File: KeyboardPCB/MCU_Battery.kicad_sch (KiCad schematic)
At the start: 22 parts, among them U1 ATmega32U4-M, U2 TPS61222DCK, U3 MCP73831-2-OT, Y1 XRCGB16M000FXN02R0

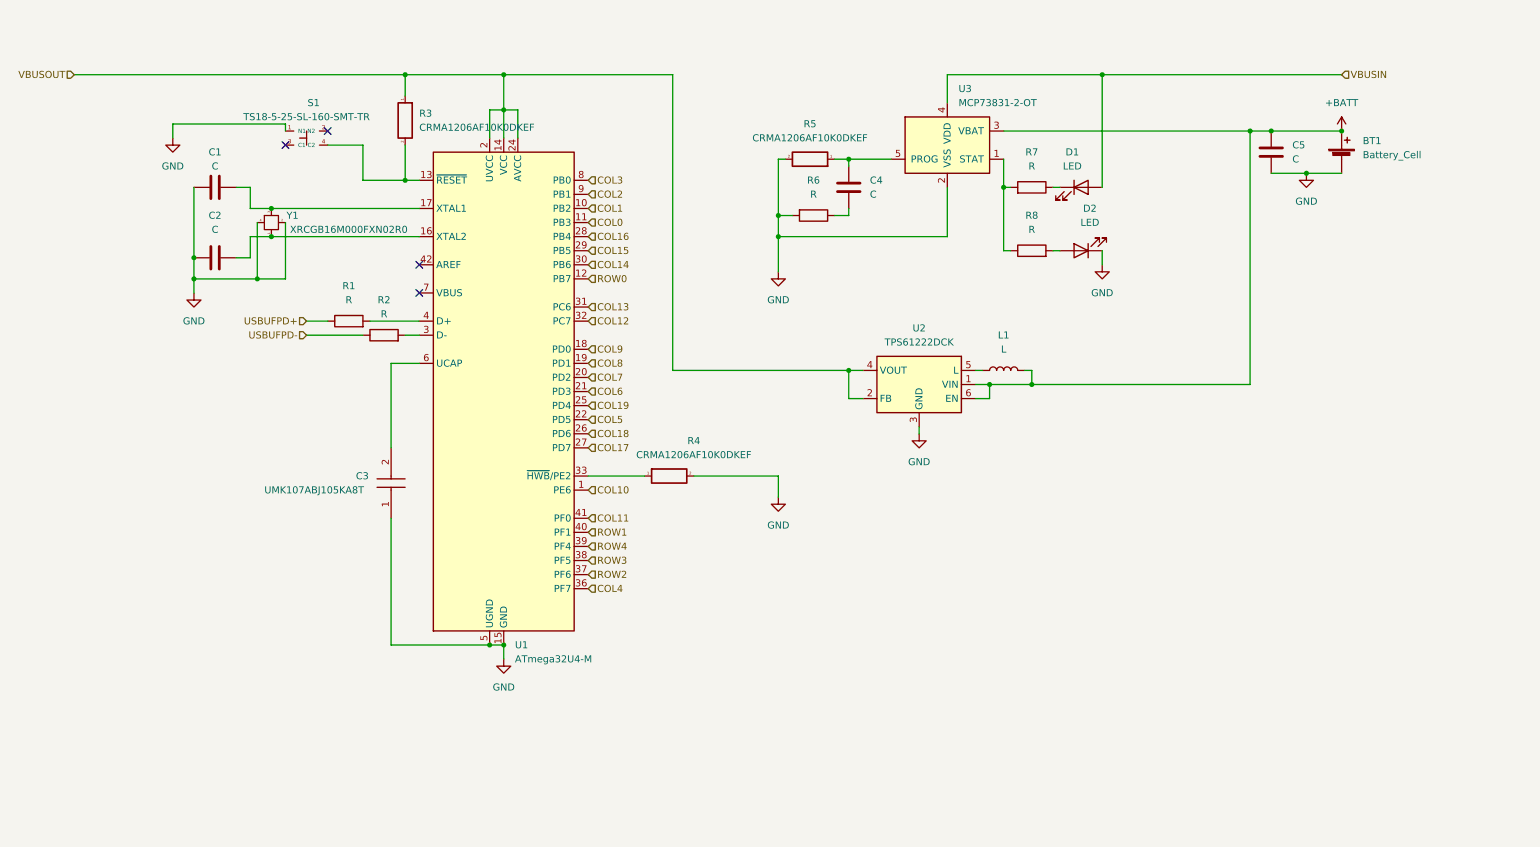
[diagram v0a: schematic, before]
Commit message: Symbol Modifications
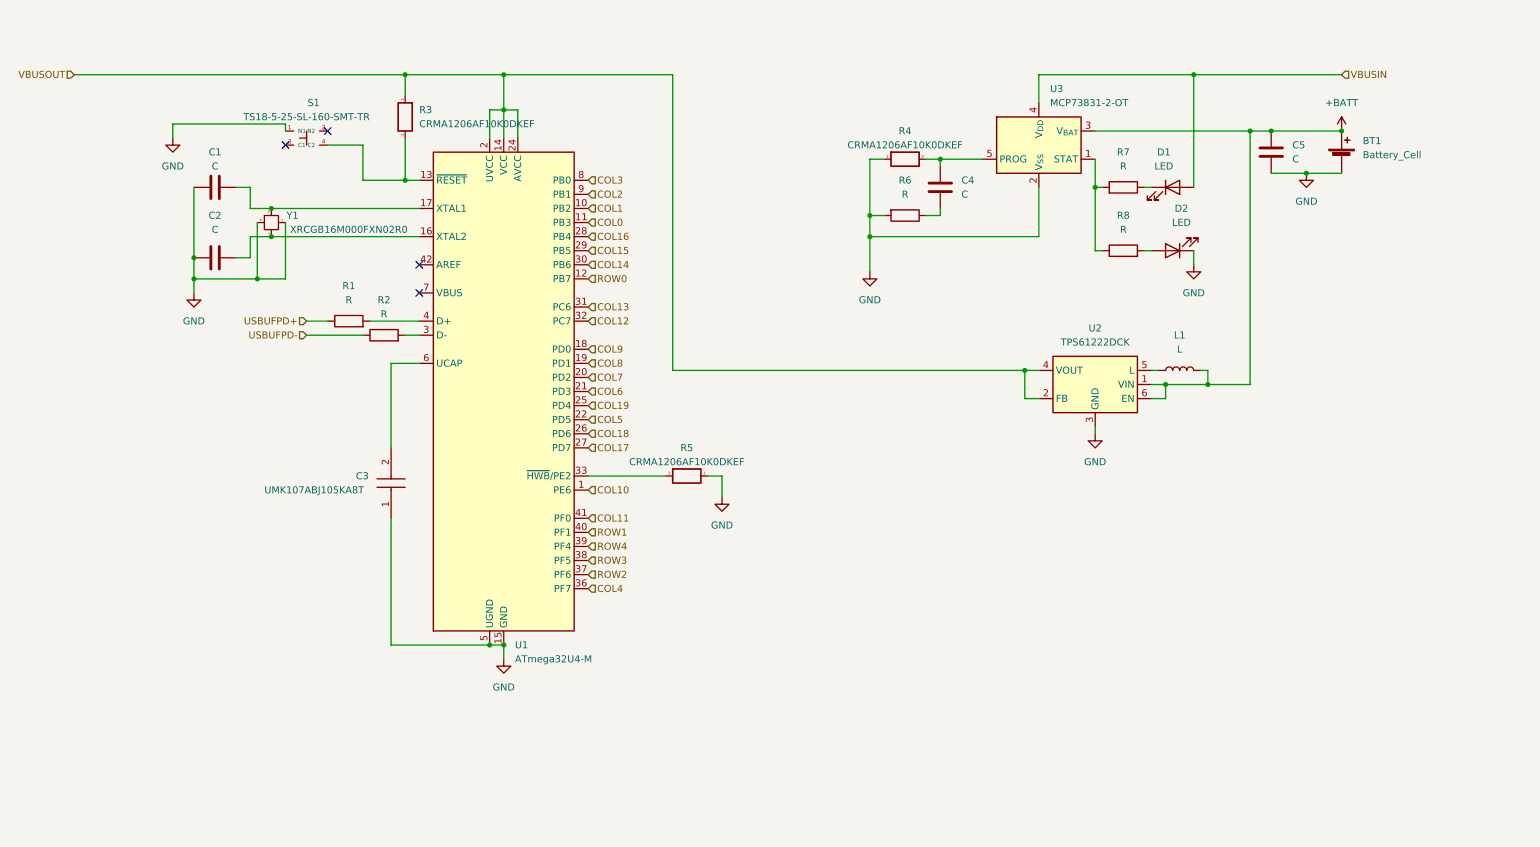
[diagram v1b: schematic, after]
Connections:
- net GND: now also R4.1; no longer R4.2
- net at U1.33 (~{HWB}/PE2): now also R5.1; no longer R4.1
- net at C4.1, U3.5 (PROG): now also R4.2; no longer R5.1
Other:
- moved on the sheet: C4, D1, D2, L1, R3, R6, R7, R8, U2, U3

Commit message: Reorganised key array
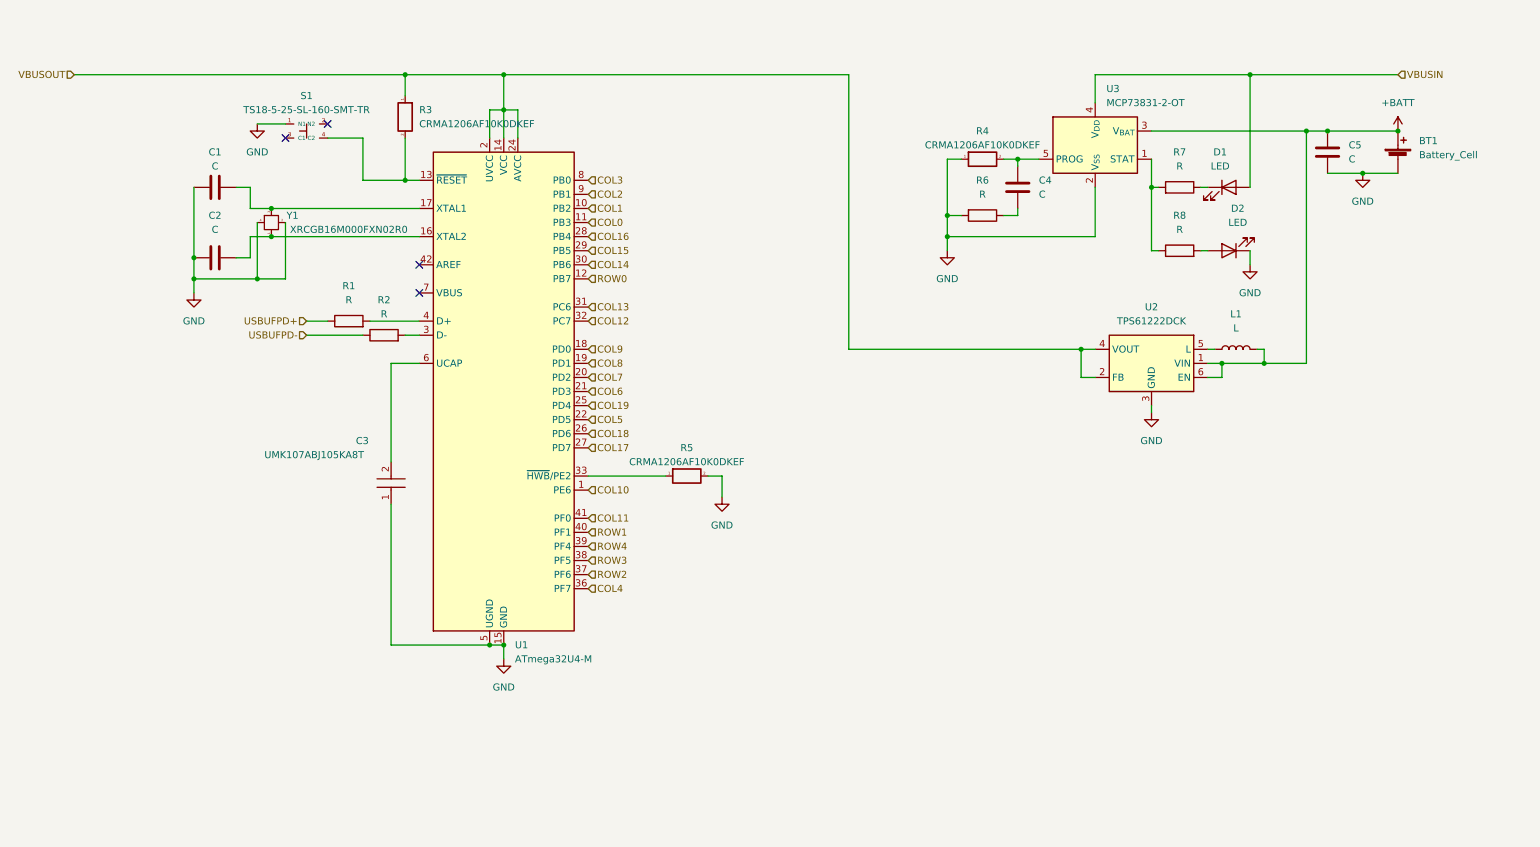
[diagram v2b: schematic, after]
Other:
- moved on the sheet: BT1, C4, C5, D1, D2, L1, R4, R6, R7, R8, S1, U2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

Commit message: Added some Capacitors
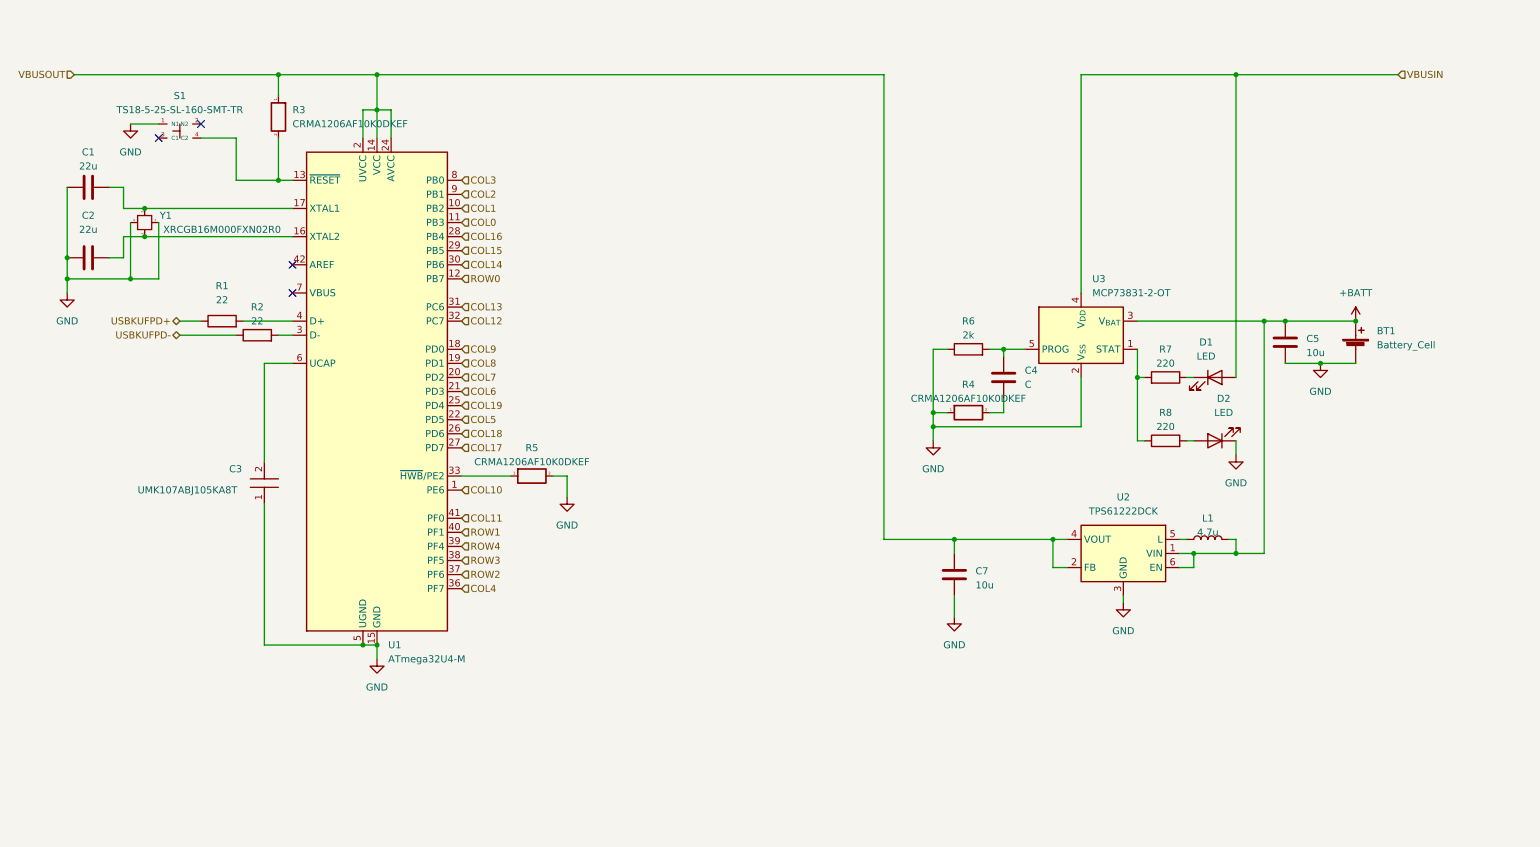
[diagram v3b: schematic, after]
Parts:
- added C7: 10u, symbol Device:C
- C1, C2: value C -> 22u
- C5: value C -> 10u
- L1: value L -> 4.7u
- R1, R2: value R -> 22
- R6: value R -> 2k
- R7, R8: value R -> 220
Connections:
- net GND: now also R6.1, C7.2; no longer R6.2
- net VBUSOUT: now also C7.1
- net at C4.2: now also R4.2; no longer R6.1
- net at C4.1, U3.5 (PROG): now also R6.2; no longer R4.2
- net USBUFPD+ renamed USBKUFPD+
- net USBUFPD- renamed USBKUFPD-
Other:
- moved on the sheet: BT1, C1, C2, C3, C4, C5, D1, D2, L1, R1, R2, R3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

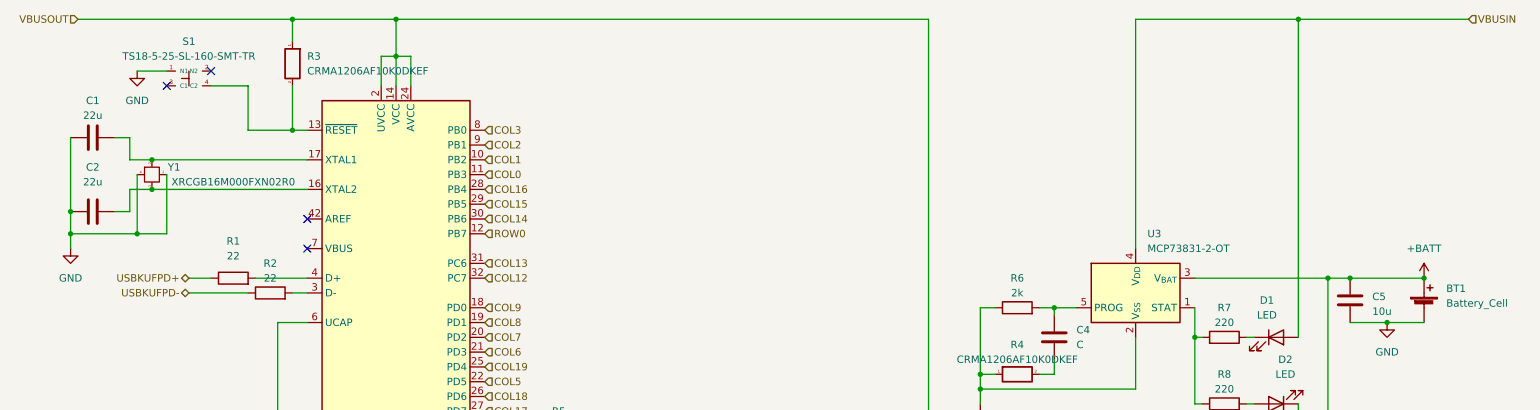
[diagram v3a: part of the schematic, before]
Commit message: added footprints and changed symbols
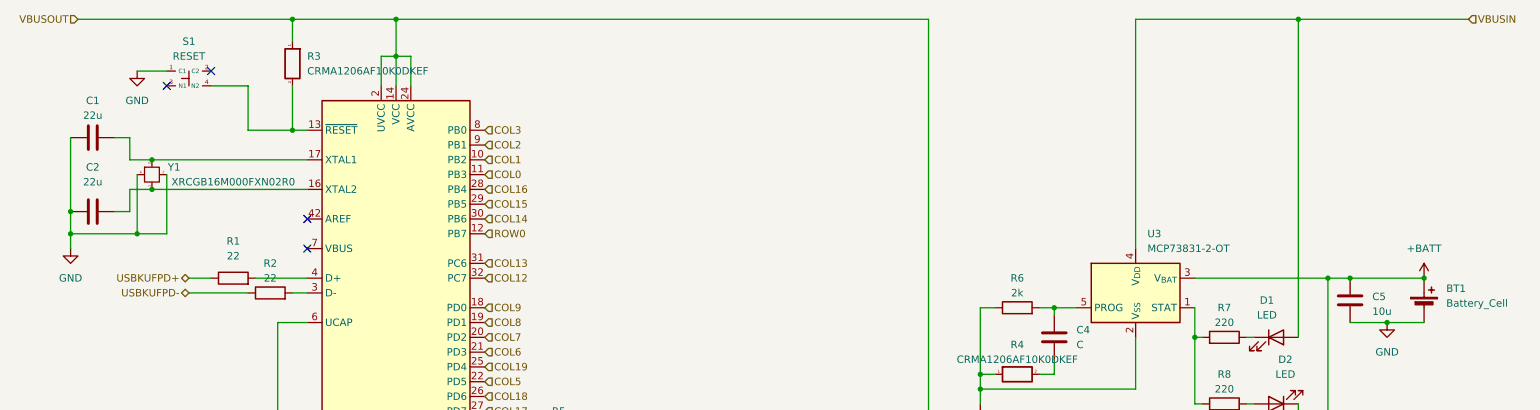
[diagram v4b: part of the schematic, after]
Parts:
- S1: value TS18-5-25-SL-160-SMT-TR -> RESET; footprint TS18525SL160SMTTR -> keyboard_syms:B3FS1012P; symbol keyboard_syms:TS18-5-25-SL-160-SMT-TR -> keyboard_syms:B3FS-1012P; Arrow Part Number (none) -> B3FS-1012P; Arrow Price/Stock (none) -> https://www.arrow.com/en/products/b3fs-1012p/omron?region=n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; Height 2.6 -> 4.3; Manufacturer_Name CUI Devices -> Omron Electronics; Manufacturer_Part_Number TS18-5-25-SL-160-SMT-TR -> B3FS-1012P; Mouser Part Number 179-TS18525SL160SMTT -> 653-B3FS-1012P; Mouser Price/Stock https://www.mouser.co.uk/ProductDetail/CUI-Devices/TS18-5-2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 -> https://www.mouser.co.uk/ProductDetail/Omron-Electronics/B3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
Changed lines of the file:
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@@
     )
   )
-  (symbol (lib_id "keyboard_syms:TS18-5-25-SL-160-SMT-TR") (at 44.45 35.56 0) (unit 1)
+  (symbol (lib_id "keyboard_syms:B3FS-1012P") (at 44.45 35.56 0) (unit 1)
     (in_bom yes) (on_board yes) (dnp no)
     (property "Reference" "S1" (at 44.45 29.21 0)
       (effects (font (size 1.27 1.27)))
     )
-    (property "Value" "TS18-5-25-SL-160-SMT-TR" (at 44.45 31.75 0)
+    (property "Value" "RESET" (at 44.45 31.75 0)
       (effects (font (size 1.27 1.27)))
     )
-    (property "Footprint" "TS18525SL160SMTTR" (at 71.12 33.02 0)
-      (effects (font (size 1.27 1.27)) (justify left) hide)
+    (property "Footprint" "keyboard_syms:B3FS1012P" (at 71.12 130.48 0)
+      (effects (font (size 1.27 1.27)) (justify left top) hide)
     )
-    (property "Datasheet" "https://www.cuidevices.com/product/resource/ts18.pdf" (at 71.12 35.56 0)
-      (effects (font (size 1.27 1.27)) (justify left) hide)
+    (property "Datasheet" "https://omronfs.omron.com/en_US/ecb/products/pdf/en-b3fs.pdf" (at 71.12 230.48 0)
+      (effects (font (size 1.27 1.27)) (justify left top) hide)
     )
     (property "Description" "Tactile Switches 5 x 5 mm, 2.5 mm Actuator Height, 160 gf, Silver, Surface Mount, TR, SPST, Tactile Switch" (at 71.12 38.1 0)
       (effects (font (size 1.27 1.27)) (justify left) hide)
     )
-    (property "Height" "2.6" (at 71.12 40.64 0)
-      (effects (font (size 1.27 1.27)) (justify left) hide)
+    (property "Height" "4.3" (at 71.12 430.48 0)
+      (effects (font (size 1.27 1.27)) (justify left top) hide)
     )
-    (property "Manufacturer_Name" "CUI Devices" (at 71.12 43.18 0)
-      (effects (font (size 1.27 1.27)) (justify left) hide)
+    (property "Manufacturer_Name" "Omron Electronics" (at 71.12 530.48 0)
+      (effects (font (size 1.27 1.27)) (justify left top) hide)
     )
-    (property "Manufacturer_Part_Number" "TS18-5-25-SL-160-SMT-TR" (at 71.12 45.72 0)
-      (effects (font (size 1.27 1.27)) (justify left) hide)
+    (property "Manufacturer_Part_Number" "B3FS-1012P" (at 71.12 630.48 0)
+      (effects (font (size 1.27 1.27)) (justify left top) hide)
     )
-    (property "Mouser Part Number" "179-TS18525SL160SMTT" (at 71.12 48.26 0)
-      (effects (font (size 1.27 1.27)) (justify left) hide)
+    (property "Mouser Part Number" "653-B3FS-1012P" (at 71.12 730.48 0)
+      (effects (font (size 1.27 1.27)) (justify left top) hide)
     )
-    (property "Mouser Price/Stock" "https://www.mouser.co.uk/ProductDetail/CUI-Devices/TS18-5-25-SL-160-SMT-TR?qs=tlsG%2FOw5FFgGURAVArQGyg%3D%3D" (at 71.12 50.8 0)
-      (effects (font (size 1.27 1.27)) (justify left) hide)
+    (property "Mouser Price/Stock" "https://www.mouser.co.uk/ProductDetail/Omron-Electronics/B3FS-1012P?qs=1tDaWCEHQQ7mwfTJVAKWQA%3D%3D" (at 71.12 830.48 0)
+      (effects (font (size 1.27 1.27)) (justify left top) hide)
     )
-    (property "Arrow Part Number" "" (at 71.12 53.34 0)
-      (effects (font (size 1.27 1.27)) (justify left) hide)
+    (property "Arrow Part Number" "B3FS-1012P" (at 71.12 930.48 0)
+      (effects (font (size 1.27 1.27)) (justify left top) hide)
     )
-    (property "Arrow Price/Stock" "" (at 71.12 55.88 0)
-      (effects (font (size 1.27 1.27)) (justify left) hide)
+    (property "Arrow Price/Stock" "https://www.arrow.com/en/products/b3fs-1012p/omron?region=nac" (at 71.12 1030.48 0)
+      (effects (font (size 1.27 1.27)) (justify left top) hide)
     )
     (property "Mouser Testing Part Number" "" (at 71.12 58.42 0)
